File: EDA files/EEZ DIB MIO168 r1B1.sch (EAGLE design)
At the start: 290 parts, among them IC1 M24C32-WMN6P, IC10 DAC7760IPWPR, IC11 DAC7760IPWPR, IC12 OPA376AIDBVR, IC13 DAC7563TDGSR, IC14 OPA2196D, IC15 BTS3408G, IC16 BTS3408G, IC17 BTS3408G, IC18 BTS3408G, IC19 74HC126PW,118, IC2 Si8641AB-B-IS1, IC20 TL431B, IC21 DG468DV-T1-E3, IC22 DG468DV-T1-E3, IC23 DG468DV-T1-E3, IC24 DG468DV-T1-E3, IC25 DG468DV-T1-E3, IC26 DG468DV-T1-E3, IC27 DG468DV-T1-E3, IC28 DG468DV-T1-E3, IC29 DG468DV-T1-E3, IC3 Si8641AB-B-IS1, IC30 DG468DV-T1-E3, IC31 DG468DV-T1-E3, IC32 DG468DV-T1-E3, IC33 DG468DV-T1-E3, IC34 DG468DV-T1-E3, IC35 OPA376AIDBVR, IC36 ADS8674IDBT, IC4 MC78L12, IC5 LP2985-5DBVR, IC6 LP2985-33DBVR, IC7 MC79L12, IC8 STM32F446ZCT6, IC9 OPA2196D, J1 4907, J2 503398-1892, Q1 2N7002PS, Q10 BSS169, Q11 BSS169, Q12 BSS169, Q13 BSS169, Q2 2N7002PS, Q3 2N7002PS, Q4 2N7002PS, Q5 2N7002PS, Q6 BSS169, Q7 BSS169, Q8 BSS169, Q9 BSS169, X1 77317-104-28LF, X2 SSW-106-02-S-S, X3 691327310016, X4 691327310016, Y1 25MHz

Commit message: BOM added
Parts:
- C16, C18, C21: device rcl:C-EUC1206 -> rcl:C-EUC0805
- C75: device rcl:C-EUC1210 -> rcl:C-EUC1206
- IC14, IC9: value OPA2196D -> OPA2196IDR
- IC2, IC3: value Si8641AB-B-IS1 -> Si8641BB-B-IS1
- IC4: value MC78L12 -> L78L12
- IC5: value LP2985-5DBVR -> LP2985-50DBVR
- IC7: value MC79L12 -> L79L12
- TVS1, TVS2, TVS3, TVS4, TVS5, TVS6, TVS7, TVS8: value PESD12VL1BA.115 -> PESD12VL1BA,115
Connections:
- removed net +5V: X1-23.1, X1-24.1

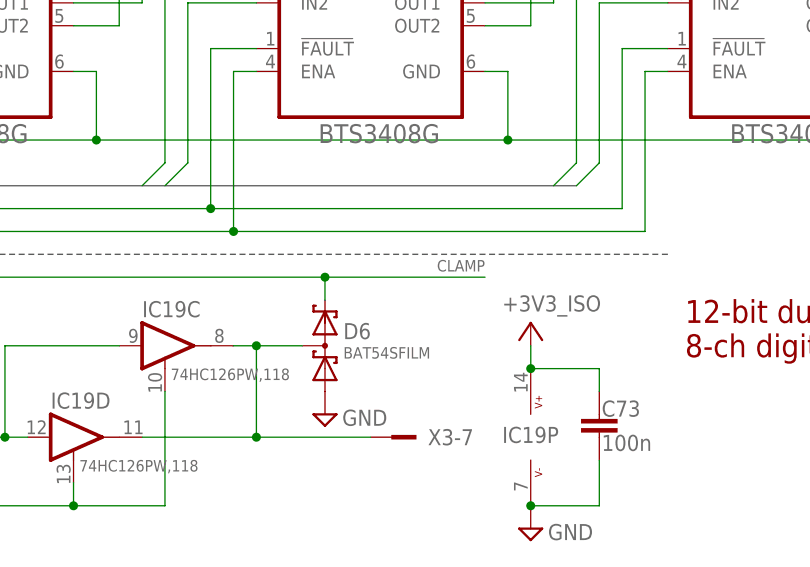
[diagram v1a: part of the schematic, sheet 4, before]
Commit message: PWM outputs clamp fix
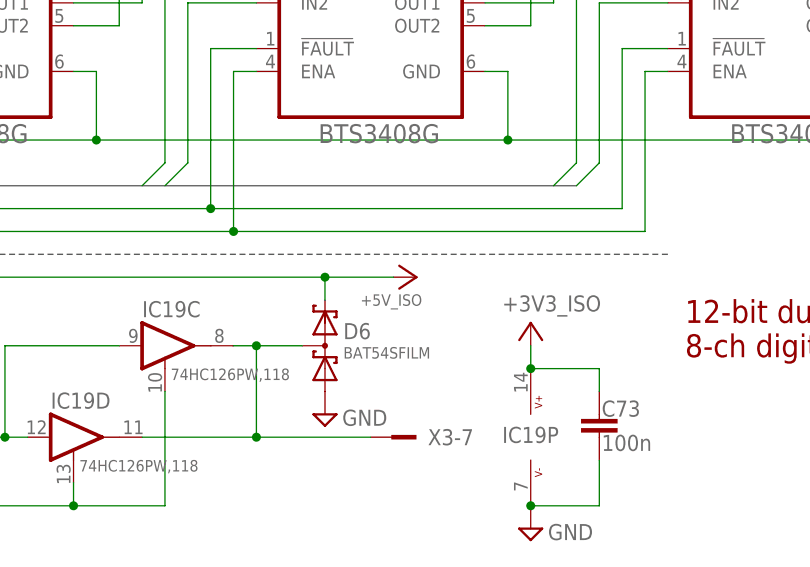
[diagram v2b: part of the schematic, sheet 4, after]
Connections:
- net +5V_ISO: now also D5.C2, D6.C2
- net CLAMP: no longer D5.C2, D6.C2
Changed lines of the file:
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@@
 <part name="U$25" library="EEZ_DIB" deviceset="+15V_ISO" device=""/>
 <part name="U$29" library="EEZ_DIB" deviceset="-15V_ISO" device=""/>
+<part name="U$31" library="EEZ_DIB" deviceset="+5V_ISO" device=""/>
 </parts>
 <sheets>
@@
 <attribute name="VALUE" x="210.947" y="131.2926" size="1.27" layer="96"/>
 </instance>
+<instance part="U$31" gate="A" x="132.08" y="35.56" smashed="yes" rot="R270">
+<attribute name="VALUE" x="135.255" y="33.655" size="1.27" layer="96" rot="R180"/>
+</instance>
 </instances>
 <busses>
@@
 </segment>
 </net>
-<net name="CLAMP" class="0">
+<net name="+5V_ISO" class="0">
 <segment>
 <pinref part="D5" gate="G$1" pin="C2"/>
 <wire x1="58.42" y1="33.02" x2="58.42" y2="35.56" width="0.1524" layer="91"/>
 <wire x1="58.42" y1="35.56" x2="124.46" y2="35.56" width="0.1524" layer="91"/>
-<label x="142.24" y="36.195" size="1.27" layer="102" rot="MR0"/>
 <pinref part="D6" gate="G$1" pin="C2"/>
-<wire x1="124.46" y1="35.56" x2="142.24" y2="35.56" width="0.1524" layer="91"/>
+<wire x1="124.46" y1="35.56" x2="132.08" y2="35.56" width="0.1524" layer="91"/>
 <wire x1="124.46" y1="33.02" x2="124.46" y2="35.56" width="0.1524" layer="91"/>
 <junction x="124.46" y="35.56"/>
+<pinref part="U$31" gate="A" pin="+5V_ISO"/>
 </segment>
 </net>

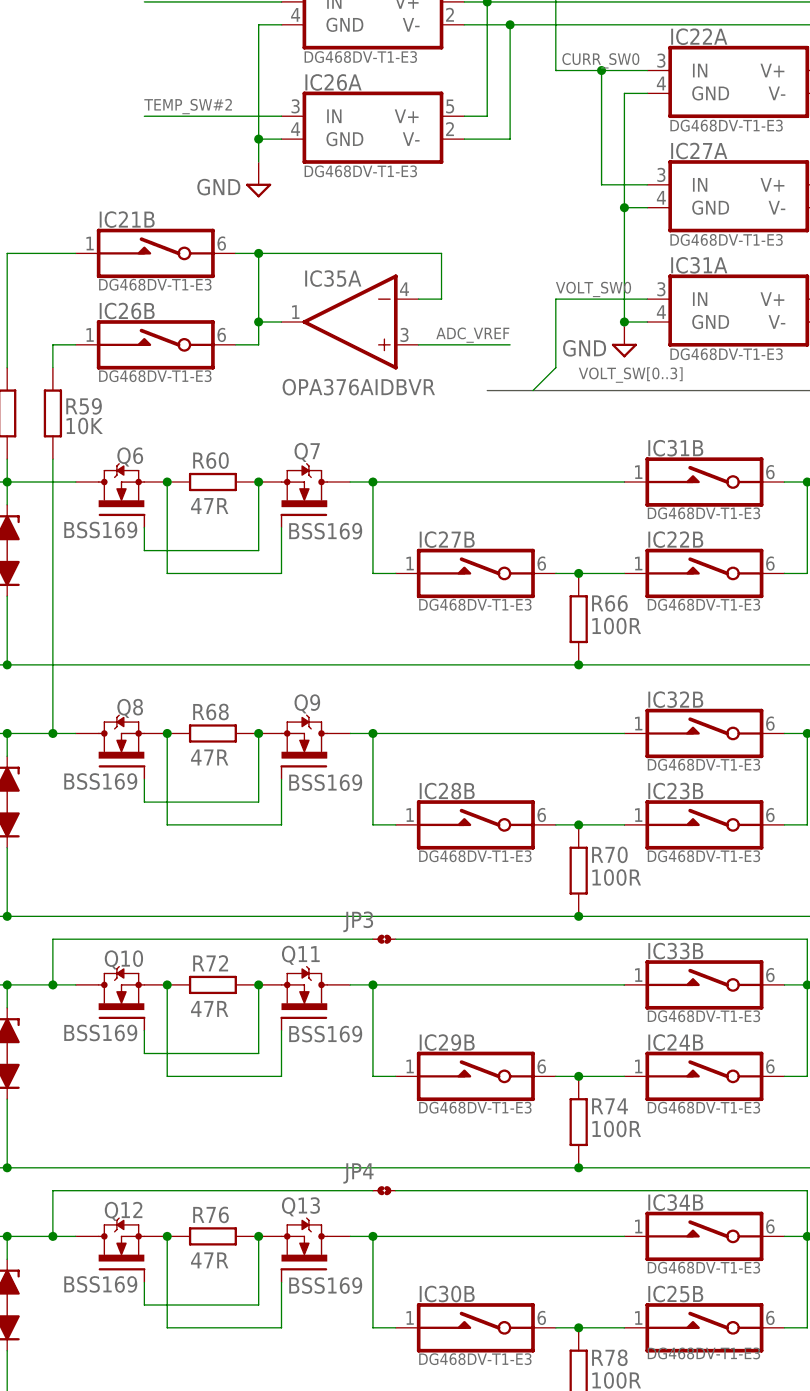
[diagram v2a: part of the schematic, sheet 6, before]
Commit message: Vref selection for NTC bias (JP3)
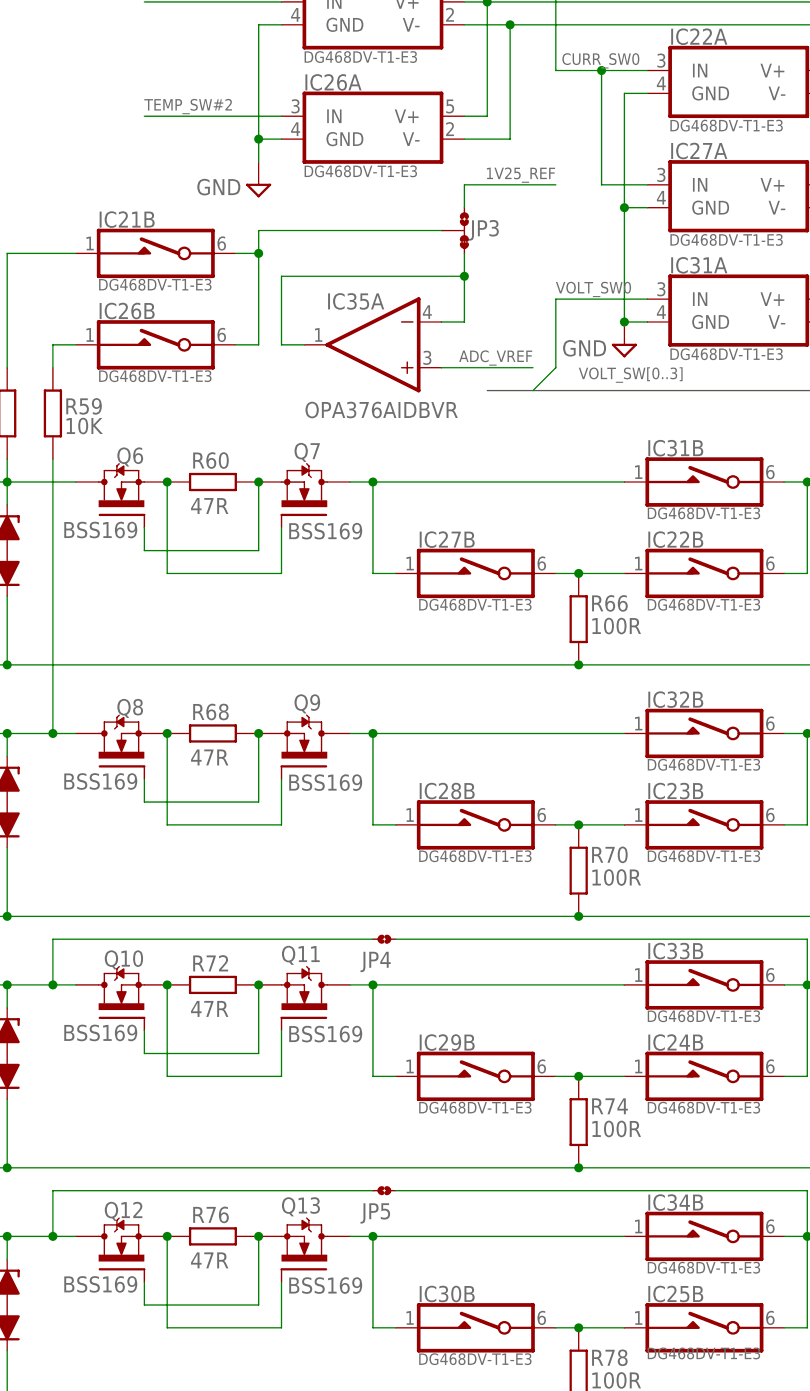
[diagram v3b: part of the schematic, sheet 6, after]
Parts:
- added JP5: JP2-CUT-0805, EEZ_Lib1:JP2-CUT-0805
- JP3: value JP2-CUT-0805 -> JP3-CUT; device EEZ_Lib1:JP2-CUT-0805 -> EEZ_Lib1:JP3-CUT
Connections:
- new net N$20: IC21B.COM, IC26B.COM, JP3.COM
- net 1V25_REF: now also JP3.NO
- net N$136: now also JP4.1; no longer JP3.1
- net N$137: now also JP5.1; no longer JP4.1
- net N$28: now also JP5.2; no longer JP4.2
- net N$31: now also JP3.NC; no longer IC21B.COM, IC26B.COM
- net N$87: now also JP4.2; no longer JP3.2
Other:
- moved on the sheet: IC35A, JP4
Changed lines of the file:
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@@
 <setting verticaltext="up"/>
 </settings>
-<grid distance="0.1" unitdist="inch" unit="inch" style="lines" multiple="1" display="no" altdistance="0.01" altunitdist="inch" altunit="inch"/>
+<grid distance="0.025" unitdist="inch" unit="inch" style="lines" multiple="4" display="no" altdistance="0.01" altunitdist="inch" altunit="inch"/>
 <layers>
 <layer number="1" name="Top" color="4" fill="1" visible="no" active="no"/>
@@
 <part name="U$7" library="EEZ_DIB" deviceset="+12V_ISO" device=""/>
 <part name="D2" library="diode" deviceset="BAT54S" device="" value="BAT54SFILM"/>
-<part name="JP3" library="EEZ_Lib1" deviceset="JP2-CUT" device="-0805"/>
 <part name="JP4" library="EEZ_Lib1" deviceset="JP2-CUT" device="-0805"/>
+<part name="JP5" library="EEZ_Lib1" deviceset="JP2-CUT" device="-0805"/>
 <part name="U$25" library="EEZ_DIB" deviceset="+15V_ISO" device=""/>
 <part name="U$29" library="EEZ_DIB" deviceset="-15V_ISO" device=""/>
 <part name="U$31" library="EEZ_DIB" deviceset="+5V_ISO" device=""/>
+<part name="JP3" library="EEZ_Lib1" deviceset="JP3-CUT" device=""/>
 </parts>
 <sheets>
@@
 <junction x="111.76" y="162.56"/>
 <junction x="127" y="162.56"/>
+<wire x1="111.76" y1="170.18" x2="121.92" y2="170.18" width="0.1524" layer="91"/>
+<junction x="111.76" y="170.18"/>
+<label x="121.92" y="170.815" size="1.27" layer="102" rot="MR0"/>
 </segment>
 </net>
@@
 <attribute name="VALUE" x="20.955" y="94.615" size="1.778" layer="96" rot="R180"/>
 </instance>
-<instance part="IC35" gate="A" x="71.12" y="134.62" smashed="yes" rot="R180">
-<attribute name="NAME" x="72.39" y="140.335" size="1.778" layer="95" rot="R180"/>
-<attribute name="VALUE" x="63.5" y="128.27" size="1.778" layer="96" rot="MR180"/>
+<instance part="IC35" gate="A" x="73.66" y="132.08" smashed="yes" rot="R180">
+<attribute name="NAME" x="74.93" y="137.795" size="1.778" layer="95" rot="R180"/>
+<attribute name="VALUE" x="66.04" y="125.73" size="1.778" layer="96" rot="MR180"/>
 </instance>
 <instance part="Q7" gate="A" x="66.04" y="114.3" smashed="yes" rot="MR90">
@@
 <instance part="X4" gate="-7" x="17.78" y="33.02"/>
 <instance part="X4" gate="-8" x="17.78" y="10.16"/>
-<instance part="JP3" gate="G$1" x="73.66" y="66.04"/>
-<instance part="JP4" gate="G$1" x="73.66" y="38.1"/>
+<instance part="JP4" gate="G$1" x="73.66" y="66.04" smashed="yes">
+<attribute name="NAME" x="72.39" y="62.865" size="1.778" layer="95"/>
+</instance>
+<instance part="JP5" gate="G$1" x="73.66" y="38.1" smashed="yes">
+<attribute name="NAME" x="72.39" y="34.925" size="1.778" layer="95"/>
+</instance>
+<instance part="JP3" gate="G$1" x="83.82" y="144.78" smashed="yes" rot="MR0">
+<attribute name="NAME" x="84.455" y="144.145" size="1.778" layer="95"/>
+</instance>
 </instances>
 <busses>
@@
 <segment>
 <pinref part="IC35" gate="A" pin="+IN"/>
-<wire x1="78.74" y1="132.08" x2="88.9" y2="132.08" width="0.1524" layer="91"/>
-<label x="88.9" y="132.715" size="1.27" layer="102" rot="MR0"/>
+<wire x1="81.28" y1="129.54" x2="91.44" y2="129.54" width="0.1524" layer="91"/>
+<label x="91.44" y="130.175" size="1.27" layer="102" rot="MR0"/>
 </segment>
 </net>
@@
 <segment>
 <pinref part="IC35" gate="A" pin="-IN"/>
-<wire x1="78.74" y1="137.16" x2="81.28" y2="137.16" width="0.1524" layer="91"/>
-<wire x1="81.28" y1="137.16" x2="81.28" y2="142.24" width="0.1524" layer="91"/>
-<wire x1="81.28" y1="142.24" x2="60.96" y2="142.24" width="0.1524" layer="91"/>
+<wire x1="81.28" y1="134.62" x2="83.82" y2="134.62" width="0.1524" layer="91"/>
+<wire x1="83.82" y1="134.62" x2="83.82" y2="139.7" width="0.1524" layer="91"/>
+<wire x1="83.82" y1="139.7" x2="63.5" y2="139.7" width="0.1524" layer="91"/>
 <pinref part="IC35" gate="A" pin="OUT"/>
-<wire x1="58.42" y1="142.24" x2="60.96" y2="142.24" width="0.1524" layer="91"/>
-<pinref part="IC21" gate="B" pin="COM"/>
-<pinref part="IC26" gate="B" pin="COM"/>
-<wire x1="58.42" y1="132.08" x2="60.96" y2="132.08" width="0.1524" layer="91"/>
-<wire x1="60.96" y1="132.08" x2="60.96" y2="134.62" width="0.1524" layer="91"/>
-<wire x1="60.96" y1="134.62" x2="60.96" y2="142.24" width="0.1524" layer="91"/>
-<junction x="60.96" y="142.24"/>
-<wire x1="63.5" y1="134.62" x2="60.96" y2="134.62" width="0.1524" layer="91"/>
-<junction x="60.96" y="134.62"/>
+<wire x1="66.04" y1="132.08" x2="63.5" y2="132.08" width="0.1524" layer="91"/>
+<wire x1="63.5" y1="132.08" x2="63.5" y2="139.7" width="0.1524" layer="91"/>
+<pinref part="JP3" gate="G$1" pin="NC"/>
+<wire x1="83.82" y1="142.24" x2="83.82" y2="139.7" width="0.1524" layer="91"/>
+<junction x="83.82" y="139.7"/>
 </segment>
 </net>
@@
 <wire x1="38.1" y1="60.96" x2="38.1" y2="66.04" width="0.1524" layer="91"/>
 <junction x="38.1" y="60.96"/>
-<pinref part="JP3" gate="G$1" pin="1"/>
+<pinref part="JP4" gate="G$1" pin="1"/>
 <wire x1="38.1" y1="66.04" x2="73.66" y2="66.04" width="0.1524" layer="91"/>
 </segment>
@@
 <junction x="33.02" y="33.02"/>
 <pinref part="FB9" gate="G$1" pin="2"/>
-<pinref part="JP4" gate="G$1" pin="1"/>
+<pinref part="JP5" gate="G$1" pin="1"/>
 <wire x1="38.1" y1="33.02" x2="33.02" y2="33.02" width="0.1524" layer="91"/>
 <wire x1="73.66" y1="38.1" x2="38.1" y2="38.1" width="0.1524" layer="91"/>
@@
 <junction x="121.92" y="33.02"/>
 <pinref part="R77" gate="G$1" pin="1"/>
-<pinref part="JP4" gate="G$1" pin="2"/>
+<pinref part="JP5" gate="G$1" pin="2"/>
 <wire x1="76.2" y1="38.1" x2="121.92" y2="38.1" width="0.1524" layer="91"/>
 <wire x1="121.92" y1="38.1" x2="121.92" y2="33.02" width="0.1524" layer="91"/>
@@
 <junction x="121.92" y="60.96"/>
 <pinref part="R73" gate="G$1" pin="1"/>
-<pinref part="JP3" gate="G$1" pin="2"/>
+<pinref part="JP4" gate="G$1" pin="2"/>
 <wire x1="76.2" y1="66.04" x2="121.92" y2="66.04" width="0.1524" layer="91"/>
 <wire x1="121.92" y1="66.04" x2="121.92" y2="60.96" width="0.1524" layer="91"/>
@@
 </segment>
 </net>
+<net name="1V25_REF" class="0">
+<segment>
+<pinref part="JP3" gate="G$1" pin="NO"/>
+<wire x1="83.82" y1="147.32" x2="83.82" y2="149.86" width="0.1524" layer="91"/>
+<wire x1="83.82" y1="149.86" x2="93.98" y2="149.86" width="0.1524" layer="91"/>
+<label x="93.98" y="150.495" size="1.27" layer="102" rot="MR0"/>
+</segment>
+</net>
+<net name="N$20" class="0">
+<segment>
+<pinref part="IC21" gate="B" pin="COM"/>
+<wire x1="58.42" y1="142.24" x2="60.96" y2="142.24" width="0.1524" layer="91"/>
+<pinref part="JP3" gate="G$1" pin="COM"/>
+<wire x1="81.28" y1="144.78" x2="60.96" y2="144.78" width="0.1524" layer="91"/>
+<wire x1="60.96" y1="144.78" x2="60.96" y2="142.24" width="0.1524" layer="91"/>
+<junction x="60.96" y="142.24"/>
+<wire x1="60.96" y1="132.08" x2="60.96" y2="142.24" width="0.1524" layer="91"/>
+<pinref part="IC26" gate="B" pin="COM"/>
+<wire x1="58.42" y1="132.08" x2="60.96" y2="132.08" width="0.1524" layer="91"/>
+</segment>
+</net>

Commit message: Changes suggested by @jbb
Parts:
- added R80, R81: 560K, rcl:R-EU_R1206
- added R82: 100R, rcl:R-EU_R0805
- added R83: 1K1, rcl:R-EU_R0805
- C97: value 4n7/1kV -> 2n2; device rcl:C-EUC1812 -> rcl:C-EUC0805
- C98: value 2n2 -> 4n7/1kV; device rcl:C-EUC0805 -> rcl:C-EUC1812
- R31, R70, R74, R78: value 100R -> 47R
- R32: value 470R -> 47R
- R33: value 1K8 -> 100R
- R34: value 2K7 -> 470R; device rcl:R-EU_R1206 -> rcl:R-EU_R0805
- R35: value 2K7 -> 1K8; device rcl:R-EU_R1206 -> rcl:R-EU_R0805
- R42, R43: value 27K -> 2K7; device rcl:R-EU_R0805 -> rcl:R-EU_R1206
- R50, R51: value 1K -> 27K
- R58, R59: value 10K -> 1K
- R60: value 47R -> 10K
- R61: value 1K -> 10K
- R62: value N.C. -> 47R
- R63: value N.C. -> 1K
- R66: value 100R -> N.C.
- R67: value 1K1 -> N.C.
- R68, R72, R76: value 47R -> 100R
- R69, R73, R77: value 1K -> 1K1
- R71, R75, R79: value 1K1 -> 1K
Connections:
- new net N$21: R80.2, R81.1
- new net N$22: R31.1, X3-6.1
- new net N$25: R32.1, X3-7.1
- net +3V3_ISO: now also R33.1; no longer R31.1
- net -12V_ISO: now also R66.1, R67.1; no longer R62.1, R63.1
- net AGND2: now also R72.1, R73.1; no longer R70.1, R71.1
- net AGND4: now also R82.1, R83.1; no longer R78.1, R79.1
- net AIN0: now also R60.2; no longer R58.2
- net AIN1: now also R61.2; no longer R59.2
- net AIN_0GND: now also R69.2; no longer R67.2
- net AIN_0P: now also R63.2, R66.2; no longer R61.2, R64.2
- net AIN_1GND: now also R73.2; no longer R71.2
- net AIN_1P: now also R64.2, R71.2; no longer R62.2, R69.2
- net AIN_2GND: now also R77.2; no longer R75.2
- net AIN_2P: now also R67.2, R75.2; no longer R65.2, R73.2
- net AIN_3GND: now also C97.1, R83.2; no longer C98.1, R79.2
- net AIN_3P: now also C97.2, R65.2, R79.2; no longer C98.2, R63.2, R77.2
- net CLAMP: now also R33.2, R34.1; no longer R31.2, R32.1
- net DIN0: now also R36.2, R44.2, R52.1; no longer R34.2, R42.2, R50.1
- net DIN1: now also R37.2, R45.2, R53.1; no longer R35.2, R43.2, R51.1
- net DIN2: now also R38.2, R46.2, R54.1; no longer R36.2, R44.2, R52.1
- net DIN3: now also R39.2, R47.2, R55.1; no longer R37.2, R45.2, R53.1
- net DIN4: now also R40.2, R48.2, R56.1; no longer R38.2, R46.2, R54.1
- net DIN5: now also R41.2, R49.2, R57.1; no longer R39.2, R47.2, R55.1
- net DIN6: now also R42.2, R50.2, R58.1; no longer R40.2, R48.2, R56.1
- net DIN7: now also R43.2, R51.2, R59.1; no longer R41.2, R49.2, R57.1
- net GND: now also C98.2, R35.2, R50.1, R51.1, R81.2; no longer C97.2, R33.2, R42.1, R43.1
- net N$10: now also R54.2; no longer R52.2
- net N$109: now also R40.1; no longer R38.1
- net N$119: now also R42.1; no longer R40.1
- net N$120: now also R43.1; no longer R41.1
- net N$122: now also R41.1; no longer R39.1
- net N$126: now also R60.1; no longer R58.1
- net N$129: now also R31.2; no longer X3-6.1
- net N$13: now also R55.2; no longer R53.2
- net N$130: now also R61.1; no longer R59.1
- net N$134: now also R32.2; no longer X3-7.1
- net N$14: now also R37.1; no longer R35.1
- net N$15: now also R56.2; no longer R54.2
- net N$16: now also R57.2; no longer R55.2
- net N$17: now also R58.2; no longer R56.2
- net N$2: now also R78.1; no longer R76.1
- net N$23: now also R59.2; no longer R57.2
- net N$28: now also R79.1; no longer R77.1
- net N$3: now also R68.1, R69.1; no longer R66.1, R67.1
- net N$32: now also R70.1; no longer R68.1
- net N$33: now also R70.2; no longer R68.2
- net N$36: now also R36.1; no longer R34.1
- net N$38: now also R38.1; no longer R36.1
- net N$4: now also R78.2; no longer R76.2
- net N$42: now also R39.1; no longer R37.1
- net N$50: now also R72.2; no longer R70.2
- net N$51: now also R71.1; no longer R69.1
- net N$6: now also R82.2; no longer R78.2
- net N$7: now also R34.2, R35.1; no longer R32.2, R33.1
- net N$77: now also R74.1; no longer R72.1
- net N$78: now also R62.1; no longer R60.1
- net N$8: now also R52.2; no longer R50.2
- net N$84: now also R74.2; no longer R72.2
- net N$85: now also R76.2; no longer R74.2
- net N$86: now also R62.2; no longer R60.2
- net N$87: now also R75.1; no longer R73.1
- net N$89: now also R68.2; no longer R66.2
- net N$9: now also R53.2; no longer R51.2
- net N$90: now also R76.1, R77.1; no longer R74.1, R75.1
- net N$92: now also R63.1; no longer R61.1
- net PE: now also C98.1, R80.1; no longer C97.1
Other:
- moved on the sheet: C97, C98, IC19A, R33, R34, R35, R36, R37, R38, R39, R40, R41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
